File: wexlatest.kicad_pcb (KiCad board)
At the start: 2 copper layers, 86 x 100 mm, 58 parts, among them J1 Screw_Terminal_01x02, J2 Conn_02x10_Odd_Even, J3 DB25_Female, J5 Conn_02x06_Odd_Even, SW10 SW_DIP_x06, SW5 SW_DIP_x01

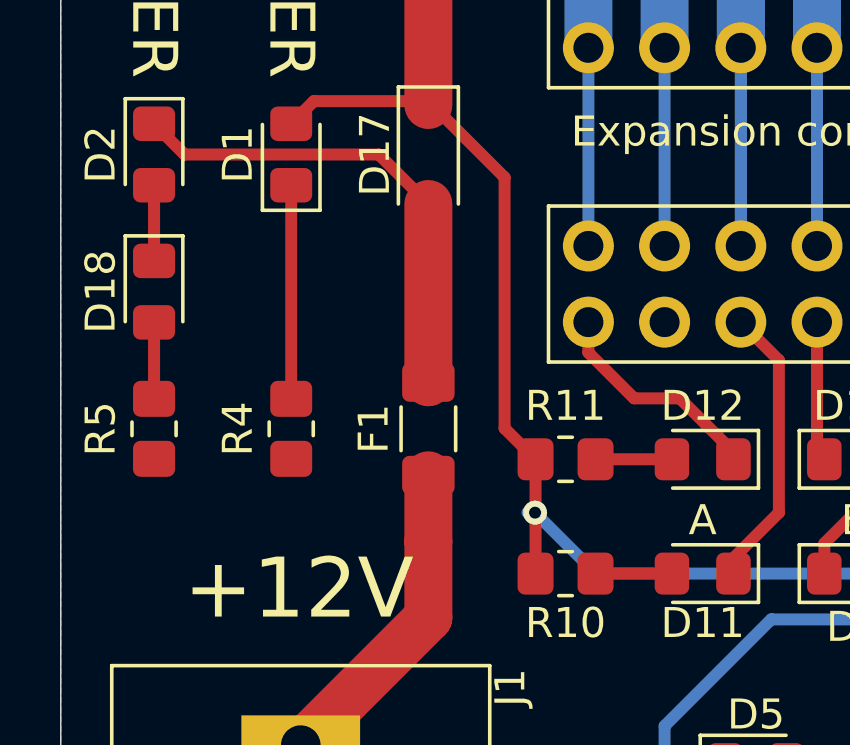
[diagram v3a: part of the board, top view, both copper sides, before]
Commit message: Change fuse package to 1812.
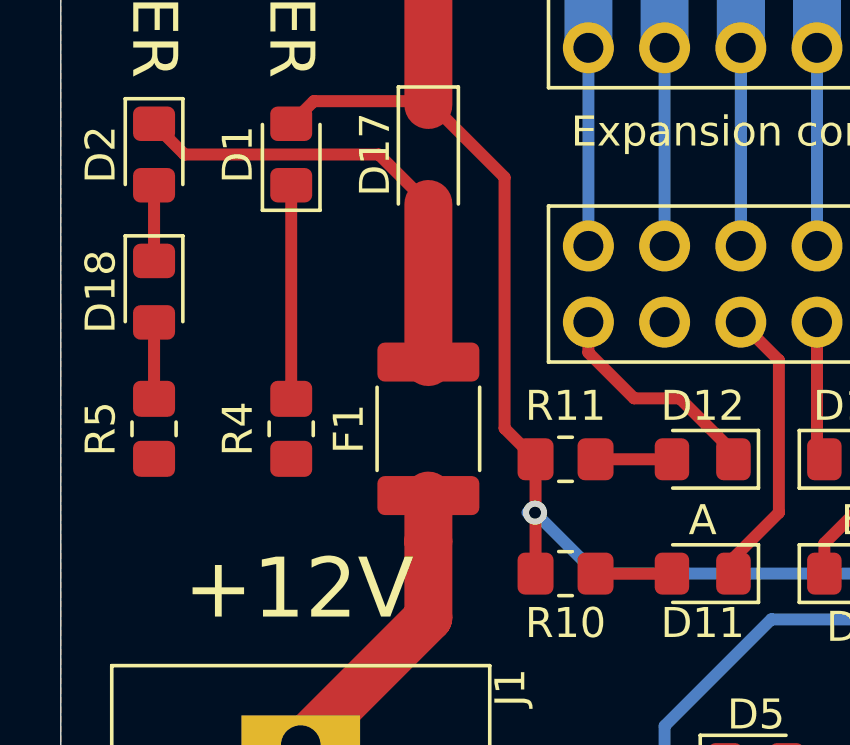
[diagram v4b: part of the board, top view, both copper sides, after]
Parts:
- F1: footprint Resistor_SMD:R_1206_3216Metric_Pad1.30x1.75mm_HandSolder -> Resistor_SMD:R_1812_4532Metric_Pad1.30x3.40mm_HandSolder
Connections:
- R1 pad 2: IN- -> IN+
- R2 pad 2: IN+ -> IN-
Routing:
- net Net-(D17-Pad2): track 16.2 -> 15.5 mm
- net Net-(F1-Pad1): track 10.8 -> 10.1 mm
